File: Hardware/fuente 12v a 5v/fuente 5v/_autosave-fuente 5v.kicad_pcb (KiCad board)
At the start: 2 copper layers, 8 parts, among them J1 Conn_01x02_Male

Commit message: Actualizacion de placas
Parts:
- removed J1: Conn_01x02_Male, Connector_PinHeader_2.54mm:PinHeader_1x02_P2.54mm_Vertical
- added REF**: TerminalBlock_bornier-2_P5.08mm, TerminalBlock:TerminalBlock_bornier-2_P5.08mm, F.Cu at (124.7, 68.1)
- added REF**: TerminalBlock_bornier-2_P5.08mm, TerminalBlock:TerminalBlock_bornier-2_P5.08mm, F.Cu at (119.6, 76.5)
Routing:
- net Net-(12v-5v1-Pad3): track 29.5 -> 38.0 mm
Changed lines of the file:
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@@
     (thickness 1.6)
     (drawings 0)
-    (tracks 19)
+    (tracks 21)
     (zones 0)
-    (modules 8)
+    (modules 9)
     (nets 5)
   )
@@
   )
   (setup
-    (last_trace_width 0.25)
+    (last_trace_width 1)
     (user_trace_width 1)
     (trace_clearance 0.2)
@@
     (mod_text_size 1 1)
     (mod_text_width 0.15)
-    (pad_size 1.524 1.524)
-    (pad_drill 0.762)
+    (pad_size 3 3)
+    (pad_drill 1.52)
     (pad_to_mask_clearance 0.051)
     (solder_mask_min_width 0.25)
@@
     (add_net "Net-(D1-Pad2)")
   )
+  (module TerminalBlock:TerminalBlock_bornier-2_P5.08mm (layer F.Cu)
+    (at 124.714 68.072 180)
+    (descr "simple 2-pin terminal block, pitch 5.08mm, revamped version of bornier2")
+    (tags "terminal block bornier2")
+    (fp_text reference REF** (at 2.54 -5.08) (layer F.SilkS)
+      (effects (font (size 1 1) (thickness 0.15)))
+    )
+    (fp_text value TerminalBlock_bornier-2_P5.08mm (at 10.414 3.302) (layer F.Fab)
+      (effects (font (size 1 1) (thickness 0.15)))
+    )
+    (fp_line (start 7.79 4) (end -2.71 4) (layer F.CrtYd) (width 0.05))
+    (fp_line (start 7.79 4) (end 7.79 -4) (layer F.CrtYd) (width 0.05))
+    (fp_line (start -2.71 -4) (end -2.71 4) (layer F.CrtYd) (width 0.05))
+    (fp_line (start -2.71 -4) (end 7.79 -4) (layer F.CrtYd) (width 0.05))
+    (fp_line (start -2.54 3.81) (end 7.62 3.81) (layer F.SilkS) (width 0.12))
+    (fp_line (start -2.54 -3.81) (end -2.54 3.81) (layer F.SilkS) (width 0.12))
+    (fp_line (start 7.62 -3.81) (end -2.54 -3.81) (layer F.SilkS) (width 0.12))
+    (fp_line (start 7.62 3.81) (end 7.62 -3.81) (layer F.SilkS) (width 0.12))
+    (fp_line (start 7.62 2.54) (end -2.54 2.54) (layer F.SilkS) (width 0.12))
+    (fp_line (start 7.54 -3.75) (end -2.46 -3.75) (layer F.Fab) (width 0.1))
+    (fp_line (start 7.54 3.75) (end 7.54 -3.75) (layer F.Fab) (width 0.1))
+    (fp_line (start -2.46 3.75) (end 7.54 3.75) (layer F.Fab) (width 0.1))
+    (fp_line (start -2.46 -3.75) (end -2.46 3.75) (layer F.Fab) (width 0.1))
+    (fp_line (start -2.41 2.55) (end 7.49 2.55) (layer F.Fab) (width 0.1))
+    (fp_text user %R (at 2.54 0) (layer F.Fab)
+      (effects (font (size 1 1) (thickness 0.15)))
+    )
+    (pad 2 thru_hole circle (at 5.08 0 180) (size 3 3) (drill 1.52) (layers *.Cu *.Mask)
+      (net 1 "Net-(12v-5v1-Pad3)"))
+    (pad 1 thru_hole rect (at 0 0 180) (size 3 3) (drill 1.52) (layers *.Cu *.Mask)
+      (net 2 GND))
+    (model ${KISYS3DMOD}/TerminalBlock.3dshapes/TerminalBlock_bornier-2_P5.08mm.wrl
+      (offset (xyz 2.539999961853027 0 0))
+      (scale (xyz 1 1 1))
+      (rotate (xyz 0 0 0))
+    )
+  )
+  (module TerminalBlock:TerminalBlock_bornier-2_P5.08mm (layer F.Cu)
+    (at 119.634 76.454)
+    (descr "simple 2-pin terminal block, pitch 5.08mm, revamped version of bornier2")
+    (tags "terminal block bornier2")
+    (fp_text reference REF** (at 2.54 -5.08) (layer F.SilkS)
+      (effects (font (size 1 1) (thickness 0.15)))
+    )
+    (fp_text value TerminalBlock_bornier-2_P5.08mm (at -5.334 3.556) (layer F.Fab)
+      (effects (font (size 1 1) (thickness 0.15)))
+    )
+    (fp_line (start 7.79 4) (end -2.71 4) (layer F.CrtYd) (width 0.05))
+    (fp_line (start 7.79 4) (end 7.79 -4) (layer F.CrtYd) (width 0.05))
+    (fp_line (start -2.71 -4) (end -2.71 4) (layer F.CrtYd) (width 0.05))
+    (fp_line (start -2.71 -4) (end 7.79 -4) (layer F.CrtYd) (width 0.05))
+    (fp_line (start -2.54 3.81) (end 7.62 3.81) (layer F.SilkS) (width 0.12))
+    (fp_line (start -2.54 -3.81) (end -2.54 3.81) (layer F.SilkS) (width 0.12))
+    (fp_line (start 7.62 -3.81) (end -2.54 -3.81) (layer F.SilkS) (width 0.12))
+    (fp_line (start 7.62 3.81) (end 7.62 -3.81) (layer F.SilkS) (width 0.12))
+    (fp_line (start 7.62 2.54) (end -2.54 2.54) (layer F.SilkS) (width 0.12))
+    (fp_line (start 7.54 -3.75) (end -2.46 -3.75) (layer F.Fab) (width 0.1))
+    (fp_line (start 7.54 3.75) (end 7.54 -3.75) (layer F.Fab) (width 0.1))
+    (fp_line (start -2.46 3.75) (end 7.54 3.75) (layer F.Fab) (width 0.1))
+    (fp_line (start -2.46 -3.75) (end -2.46 3.75) (layer F.Fab) (width 0.1))
+    (fp_line (start -2.41 2.55) (end 7.49 2.55) (layer F.Fab) (width 0.1))
+    (fp_text user %R (at 2.54 0) (layer F.Fab)
+      (effects (font (size 1 1) (thickness 0.15)))
+    )
+    (pad 2 thru_hole circle (at 5.08 0) (size 3 3) (drill 1.52) (layers *.Cu *.Mask)
+      (net 2 GND))
+    (pad 1 thru_hole rect (at 0 0) (size 3 3) (drill 1.52) (layers *.Cu *.Mask)
+      (net 1 "Net-(12v-5v1-Pad3)"))
+    (model ${KISYS3DMOD}/TerminalBlock.3dshapes/TerminalBlock_bornier-2_P5.08mm.wrl
+      (offset (xyz 2.539999961853027 0 0))
+      (scale (xyz 1 1 1))
+      (rotate (xyz 0 0 0))
+    )
+  )
   (module Capacitor_THT:C_Disc_D3.8mm_W2.6mm_P2.50mm (layer F.Cu)
     (at 90.17 75.565)
@@
       (net 3 "Net-(12v-5v1-Pad1)"))
     (model ${KISYS3DMOD}/Capacitor_THT.3dshapes/C_Disc_D3.8mm_W2.6mm_P2.50mm.wrl
-      (at (xyz 0 0 0))
-      (scale (xyz 1 1 1))
-      (rotate (xyz 0 0 0))
-    )
-  )
-  (module Connector_PinHeader_2.54mm:PinHeader_1x02_P2.54mm_Vertical (layer F.Cu)
-    (at 119.38 71.755)
-    (descr "Through hole straight pin header, 1x02, 2.54mm pitch, single row")
-    (tags "Through hole pin header THT 1x02 2.54mm single row")
-    (fp_text reference J1 (at 0 -2.33) (layer F.SilkS)
-      (effects (font (size 1 1) (thickness 0.15)))
-    )
-    (fp_text value Conn_01x02_Male (at 0 4.87) (layer F.Fab)
-      (effects (font (size 1 1) (thickness 0.15)))
-    )
-    (fp_text user %R (at 0 1.27 90) (layer F.Fab)
-      (effects (font (size 1 1) (thickness 0.15)))
-    )
-    (fp_line (start 1.8 -1.8) (end -1.8 -1.8) (layer F.CrtYd) (width 0.05))
-    (fp_line (start 1.8 4.35) (end 1.8 -1.8) (layer F.CrtYd) (width 0.05))
-    (fp_line (start -1.8 4.35) (end 1.8 4.35) (layer F.CrtYd) (width 0.05))
-    (fp_line (start -1.8 -1.8) (end -1.8 4.35) (layer F.CrtYd) (width 0.05))
-    (fp_line (start -1.33 -1.33) (end 0 -1.33) (layer F.SilkS) (width 0.12))
-    (fp_line (start -1.33 0) (end -1.33 -1.33) (layer F.SilkS) (width 0.12))
-    (fp_line (start -1.33 1.27) (end 1.33 1.27) (layer F.SilkS) (width 0.12))
-    (fp_line (start 1.33 1.27) (end 1.33 3.87) (layer F.SilkS) (width 0.12))
-    (fp_line (start -1.33 1.27) (end -1.33 3.87) (layer F.SilkS) (width 0.12))
-    (fp_line (start -1.33 3.87) (end 1.33 3.87) (layer F.SilkS) (width 0.12))
-    (fp_line (start -1.27 -0.635) (end -0.635 -1.27) (layer F.Fab) (width 0.1))
-    (fp_line (start -1.27 3.81) (end -1.27 -0.635) (layer F.Fab) (width 0.1))
-    (fp_line (start 1.27 3.81) (end -1.27 3.81) (layer F.Fab) (width 0.1))
-    (fp_line (start 1.27 -1.27) (end 1.27 3.81) (layer F.Fab) (width 0.1))
-    (fp_line (start -0.635 -1.27) (end 1.27 -1.27) (layer F.Fab) (width 0.1))
-    (pad 2 thru_hole oval (at 0 2.54) (size 1.7 1.7) (drill 1) (layers *.Cu *.Mask)
-      (net 1 "Net-(12v-5v1-Pad3)"))
-    (pad 1 thru_hole rect (at 0 0) (size 1.7 1.7) (drill 1) (layers *.Cu *.Mask)
-      (net 2 GND))
-    (model ${KISYS3DMOD}/Connector_PinHeader_2.54mm.3dshapes/PinHeader_1x02_P2.54mm_Vertical.wrl
       (at (xyz 0 0 0))
       (scale (xyz 1 1 1))
@@
   )
   (segment (start 97.79 69.215) (end 100.965 69.215) (width 1) (layer B.Cu) (net 1))
-  (segment (start 113.03 77.47) (end 108.585 77.47) (width 1) (layer B.Cu) (net 1))
   (segment (start 102.430001 72.585001) (end 102.430001 75.815001) (width 1) (layer B.Cu) (net 1))
-  (segment (start 108.585 77.47) (end 106.68 75.565) (width 1) (layer B.Cu) (net 1))
-  (segment (start 119.38 74.295) (end 116.205 74.295) (width 1) (layer B.Cu) (net 1))
   (segment (start 106.429999 75.815001) (end 106.68 75.565) (width 1) (layer B.Cu) (net 1))
   (segment (start 100.965 69.215) (end 100.965 71.12) (width 1) (layer B.Cu) (net 1))
   (segment (start 100.965 71.12) (end 102.430001 72.585001) (width 1) (layer B.Cu) (net 1))
-  (segment (start 116.205 74.295) (end 113.03 77.47) (width 1) (layer B.Cu) (net 1))
   (segment (start 102.430001 75.815001) (end 106.429999 75.815001) (width 1) (layer B.Cu) (net 1))
+  (segment (start 117.134 76.454) (end 119.634 76.454) (width 1) (layer B.Cu) (net 1))
+  (segment (start 107.95 77.724) (end 115.864 77.724) (width 1) (layer B.Cu) (net 1))
+  (segment (start 115.864 77.724) (end 117.134 76.454) (width 1) (layer B.Cu) (net 1))
+  (segment (start 106.68 75.565) (end 106.68 76.454) (width 1) (layer B.Cu) (net 1))
+  (segment (start 106.68 76.454) (end 107.95 77.724) (width 1) (layer B.Cu) (net 1))
+  (segment (start 119.634 68.072) (end 119.634 76.454) (width 1) (layer B.Cu) (net 1))
   (segment (start 90.17 69.215) (end 85.09 69.215) (width 1) (layer B.Cu) (net 3))
   (segment (start 92.75 69.215) (end 92.07 69.215) (width 1) (layer B.Cu) (net 3))
@@
     (polygon
       (pts
-        (xy 77.47 65.405) (xy 122.555 65.405) (xy 122.555 79.375) (xy 77.47 79.375)
+        (xy 78.74 63.5) (xy 128.27 63.5) (xy 128.27 81.28) (xy 78.74 81.28)
       )
     )

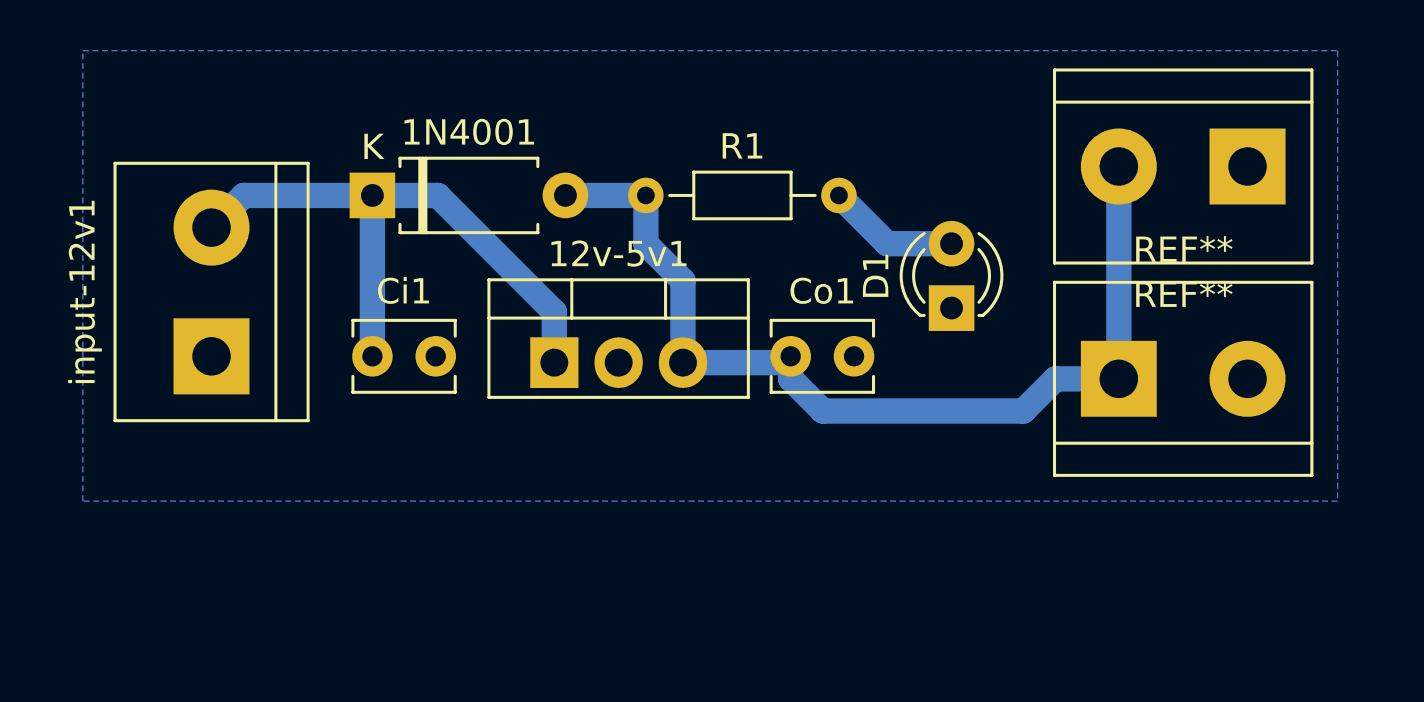
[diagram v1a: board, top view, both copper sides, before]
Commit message: Agregar USB y errores de impresion
Agregue un conector USB al regulador de 5V y corregí los errores de impresión
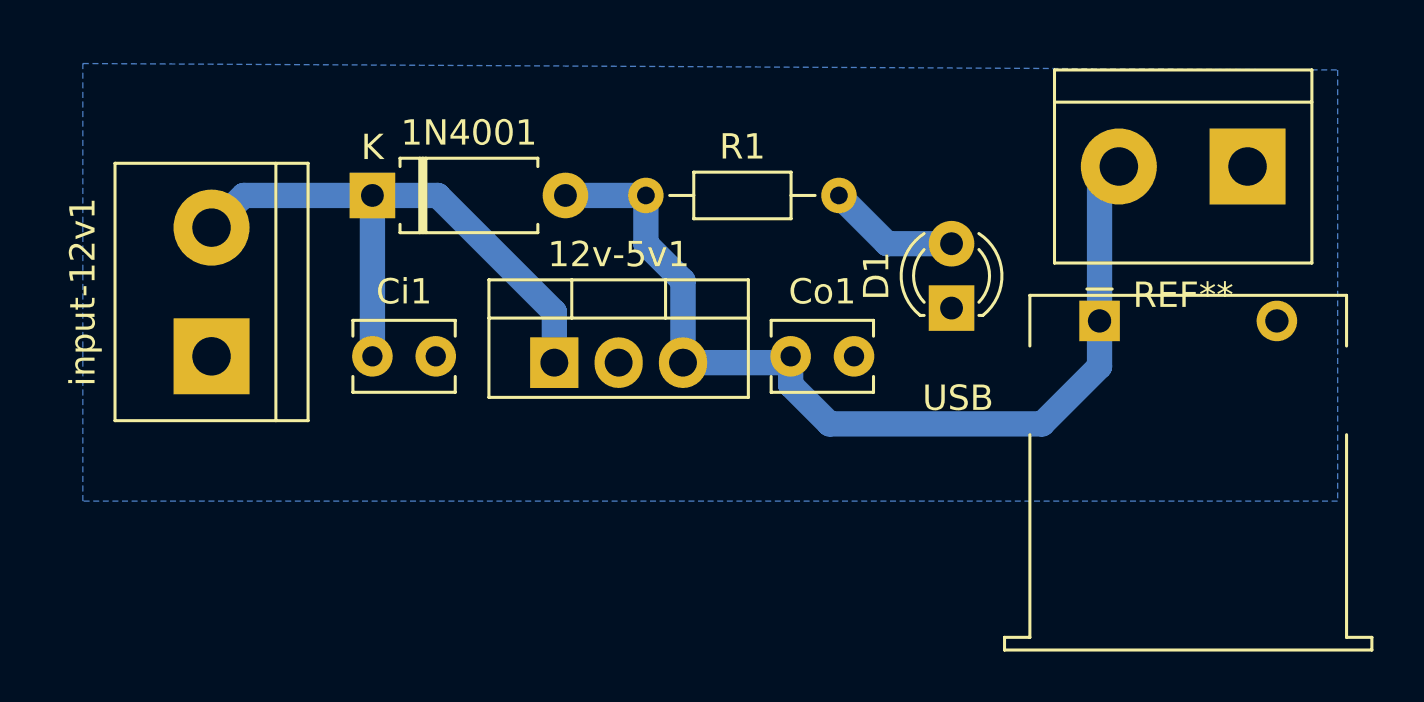
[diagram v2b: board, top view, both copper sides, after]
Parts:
- removed the REF** at (119.6, 76.5)
- added USB: USB_A_Stewart_SS-52100-001_Horizontal, Connector_USB:USB_A_Stewart_SS-52100-001_Horizontal, F.Cu at (118.9, 74.2)
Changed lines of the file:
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@@
     (thickness 1.6)
     (drawings 0)
-    (tracks 21)
+    (tracks 22)
     (zones 0)
     (modules 9)
@@
     (mod_text_size 1 1)
     (mod_text_width 0.15)
-    (pad_size 3 3)
-    (pad_drill 1.52)
+    (pad_size 1.6 1.6)
+    (pad_drill 0.92)
     (pad_to_mask_clearance 0.051)
     (solder_mask_min_width 0.25)
@@
     (add_net "Net-(D1-Pad2)")
   )
+  (module Connector_USB:USB_A_Stewart_SS-52100-001_Horizontal (layer F.Cu)
+    (at 118.872 74.168)
+    (descr "USB A connector https://belfuse.com/resources/drawings/stewartconnector/dr-stw-ss-52100-001.pdf")
+    (tags "USB_A Female Connector receptacle")
+    (fp_text reference USB (at -5.588 3.048) (layer F.SilkS)
+      (effects (font (size 1 1) (thickness 0.15)))
+    )
+    (fp_text value USB_A_Stewart_SS-52100-001_Horizontal (at -7.112 5.842) (layer F.Fab)
+      (effects (font (size 1 1) (thickness 0.15)))
+    )
+    (fp_line (start -3.25 4.74) (end -3.25 -1.51) (layer F.CrtYd) (width 0.05))
+    (fp_line (start 10.25 -1.51) (end -3.25 -1.51) (layer F.CrtYd) (width 0.05))
+    (fp_line (start 10.25 0.69) (end 10.25 -1.51) (layer F.CrtYd) (width 0.05))
+    (fp_line (start 10.75 12.49) (end 10.75 12.99) (layer F.Fab) (width 0.1))
+    (fp_line (start 9.75 12.49) (end 10.75 12.49) (layer F.Fab) (width 0.1))
+    (fp_line (start -3.75 12.49) (end -2.75 12.49) (layer F.Fab) (width 0.1))
+    (fp_line (start -3.75 12.99) (end -3.75 12.49) (layer F.Fab) (width 0.1))
+    (fp_line (start -3.75 12.99) (end 10.75 12.99) (layer F.Fab) (width 0.1))
+    (fp_line (start -2.75 12.49) (end -2.75 -1.01) (layer F.Fab) (width 0.1))
+    (fp_line (start -2.75 -1.01) (end 9.75 -1.01) (layer F.Fab) (width 0.1))
+    (fp_line (start 9.75 12.49) (end 9.75 -1.01) (layer F.Fab) (width 0.1))
+    (fp_text user %R (at 3.5 5.99) (layer F.Fab)
+      (effects (font (size 1 1) (thickness 0.15)))
+    )
+    (fp_line (start -3.75 12.99) (end 10.75 12.99) (layer F.SilkS) (width 0.12))
+    (fp_line (start 10.75 12.99) (end 10.75 12.49) (layer F.SilkS) (width 0.12))
+    (fp_line (start 10.75 12.49) (end 9.75 12.49) (layer F.SilkS) (width 0.12))
+    (fp_line (start 9.75 12.49) (end 9.75 4.49) (layer F.SilkS) (width 0.12))
+    (fp_line (start 9.75 0.99) (end 9.75 -1.01) (layer F.SilkS) (width 0.12))
+    (fp_line (start 9.75 -1.01) (end -2.75 -1.01) (layer F.SilkS) (width 0.12))
+    (fp_line (start -2.75 -1.01) (end -2.75 0.99) (layer F.SilkS) (width 0.12))
+    (fp_line (start -2.75 4.49) (end -2.75 12.49) (layer F.SilkS) (width 0.12))
+    (fp_line (start -2.75 12.49) (end -3.75 12.49) (layer F.SilkS) (width 0.12))
+    (fp_line (start -3.75 12.49) (end -3.75 12.99) (layer F.SilkS) (width 0.12))
+    (fp_line (start -0.5 -1.26) (end 0.5 -1.26) (layer F.SilkS) (width 0.12))
+    (fp_line (start -0.25 -1.01) (end 0 -0.76) (layer F.Fab) (width 0.1))
+    (fp_line (start 0 -0.76) (end 0.25 -1.01) (layer F.Fab) (width 0.1))
+    (fp_line (start -3.25 4.74) (end -3.25 11.99) (layer F.CrtYd) (width 0.05))
+    (fp_line (start -3.25 11.99) (end -4.25 11.99) (layer F.CrtYd) (width 0.05))
+    (fp_line (start -4.25 11.99) (end -4.25 13.49) (layer F.CrtYd) (width 0.05))
+    (fp_line (start -4.25 13.49) (end 11.25 13.49) (layer F.CrtYd) (width 0.05))
+    (fp_line (start 11.25 13.49) (end 11.25 11.99) (layer F.CrtYd) (width 0.05))
+    (fp_line (start 11.25 11.99) (end 10.25 11.99) (layer F.CrtYd) (width 0.05))
+    (fp_line (start 10.25 11.99) (end 10.25 0.69) (layer F.CrtYd) (width 0.05))
+    (pad 4 thru_hole circle (at 7 0) (size 1.6 1.6) (drill 0.92) (layers *.Cu *.Mask)
+      (net 2 GND))
+    (pad 1 thru_hole rect (at 0 0) (size 1.6 1.6) (drill 0.92) (layers *.Cu *.Mask)
+      (net 1 "Net-(12v-5v1-Pad3)"))
+    (model ${KISYS3DMOD}/Connector_USB.3dshapes/USB_A_Stewart_SS-52100-001_Horizontal.wrl
+      (at (xyz 0 0 0))
+      (scale (xyz 1 1 1))
+      (rotate (xyz 0 0 0))
+    )
+  )
   (module TerminalBlock:TerminalBlock_bornier-2_P5.08mm (layer F.Cu)
     (at 124.714 68.072 180)
@@
     (pad 1 thru_hole rect (at 0 0 180) (size 3 3) (drill 1.52) (layers *.Cu *.Mask)
       (net 2 GND))
-    (model ${KISYS3DMOD}/TerminalBlock.3dshapes/TerminalBlock_bornier-2_P5.08mm.wrl
-      (offset (xyz 2.539999961853027 0 0))
-      (scale (xyz 1 1 1))
-      (rotate (xyz 0 0 0))
-    )
-  )
-  (module TerminalBlock:TerminalBlock_bornier-2_P5.08mm (layer F.Cu)
-    (at 119.634 76.454)
-    (descr "simple 2-pin terminal block, pitch 5.08mm, revamped version of bornier2")
-    (tags "terminal block bornier2")
-    (fp_text reference REF** (at 2.54 -5.08) (layer F.SilkS)
-      (effects (font (size 1 1) (thickness 0.15)))
-    )
-    (fp_text value TerminalBlock_bornier-2_P5.08mm (at -5.334 3.556) (layer F.Fab)
-      (effects (font (size 1 1) (thickness 0.15)))
-    )
-    (fp_line (start 7.79 4) (end -2.71 4) (layer F.CrtYd) (width 0.05))
-    (fp_line (start 7.79 4) (end 7.79 -4) (layer F.CrtYd) (width 0.05))
-    (fp_line (start -2.71 -4) (end -2.71 4) (layer F.CrtYd) (width 0.05))
-    (fp_line (start -2.71 -4) (end 7.79 -4) (layer F.CrtYd) (width 0.05))
-    (fp_line (start -2.54 3.81) (end 7.62 3.81) (layer F.SilkS) (width 0.12))
-    (fp_line (start -2.54 -3.81) (end -2.54 3.81) (layer F.SilkS) (width 0.12))
-    (fp_line (start 7.62 -3.81) (end -2.54 -3.81) (layer F.SilkS) (width 0.12))
-    (fp_line (start 7.62 3.81) (end 7.62 -3.81) (layer F.SilkS) (width 0.12))
-    (fp_line (start 7.62 2.54) (end -2.54 2.54) (layer F.SilkS) (width 0.12))
-    (fp_line (start 7.54 -3.75) (end -2.46 -3.75) (layer F.Fab) (width 0.1))
-    (fp_line (start 7.54 3.75) (end 7.54 -3.75) (layer F.Fab) (width 0.1))
-    (fp_line (start -2.46 3.75) (end 7.54 3.75) (layer F.Fab) (width 0.1))
-    (fp_line (start -2.46 -3.75) (end -2.46 3.75) (layer F.Fab) (width 0.1))
-    (fp_line (start -2.41 2.55) (end 7.49 2.55) (layer F.Fab) (width 0.1))
-    (fp_text user %R (at 2.54 0) (layer F.Fab)
-      (effects (font (size 1 1) (thickness 0.15)))
-    )
-    (pad 2 thru_hole circle (at 5.08 0) (size 3 3) (drill 1.52) (layers *.Cu *.Mask)
-      (net 2 GND))
-    (pad 1 thru_hole rect (at 0 0) (size 3 3) (drill 1.52) (layers *.Cu *.Mask)
-      (net 1 "Net-(12v-5v1-Pad3)"))
     (model ${KISYS3DMOD}/TerminalBlock.3dshapes/TerminalBlock_bornier-2_P5.08mm.wrl
       (offset (xyz 2.539999961853027 0 0))
@@
   (segment (start 100.965 71.12) (end 102.430001 72.585001) (width 1) (layer B.Cu) (net 1))
   (segment (start 102.430001 75.815001) (end 106.429999 75.815001) (width 1) (layer B.Cu) (net 1))
-  (segment (start 117.134 76.454) (end 119.634 76.454) (width 1) (layer B.Cu) (net 1))
-  (segment (start 107.95 77.724) (end 115.864 77.724) (width 1) (layer B.Cu) (net 1))
-  (segment (start 115.864 77.724) (end 117.134 76.454) (width 1) (layer B.Cu) (net 1))
-  (segment (start 106.68 75.565) (end 106.68 76.454) (width 1) (layer B.Cu) (net 1))
-  (segment (start 106.68 76.454) (end 107.95 77.724) (width 1) (layer B.Cu) (net 1))
-  (segment (start 119.634 68.072) (end 119.634 76.454) (width 1) (layer B.Cu) (net 1))
+  (segment (start 116.608 78.232) (end 118.872 75.968) (width 1) (layer B.Cu) (net 1))
+  (segment (start 108.21563 78.232) (end 116.608 78.232) (width 1) (layer B.Cu) (net 1))
+  (segment (start 118.872 75.968) (end 118.872 74.168) (width 1) (layer B.Cu) (net 1))
+  (segment (start 106.68 75.565) (end 106.68 76.69637) (width 1) (layer B.Cu) (net 1))
+  (segment (start 106.68 76.69637) (end 108.21563 78.232) (width 1) (layer B.Cu) (net 1))
+  (segment (start 118.872 68.834) (end 119.634 68.072) (width 1) (layer B.Cu) (net 1))
+  (segment (start 118.872 74.168) (end 118.872 68.834) (width 1) (layer B.Cu) (net 1))
   (segment (start 90.17 69.215) (end 85.09 69.215) (width 1) (layer B.Cu) (net 3))
   (segment (start 92.75 69.215) (end 92.07 69.215) (width 1) (layer B.Cu) (net 3))
@@
     (polygon
       (pts
-        (xy 78.74 63.5) (xy 128.27 63.5) (xy 128.27 81.28) (xy 78.74 81.28)
+        (xy 78.74 64.008) (xy 128.27 64.262) (xy 128.27 81.28) (xy 78.74 81.28)
       )
     )
